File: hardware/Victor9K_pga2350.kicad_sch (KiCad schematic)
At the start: 28 parts, among them IC1 74LVC1G14GW,125, J1 PICO DEBUG, J2 Micro_SD_Card, J4 DX07S016JA1R1500, J5 UART, SW1 BOOTSEL, U1 ESP32-S3-DevKitC

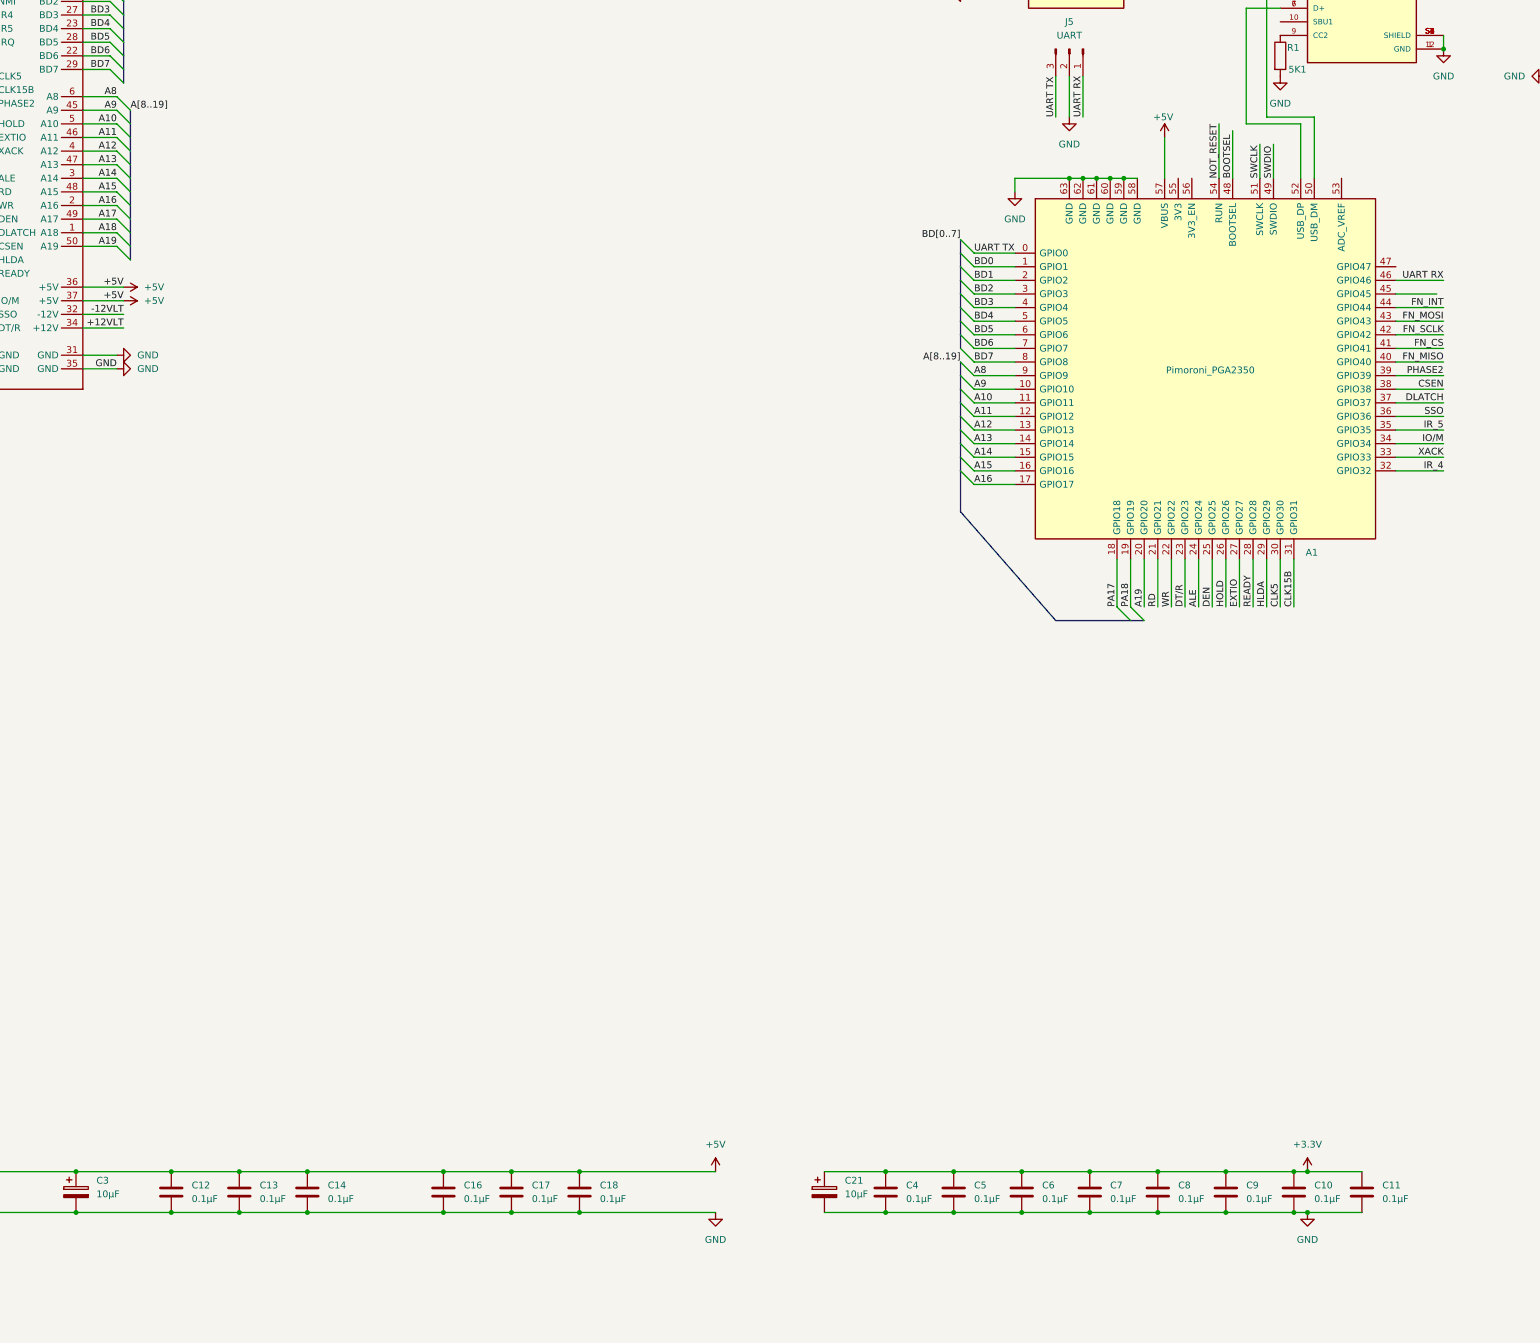
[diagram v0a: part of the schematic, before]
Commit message: initial version of re-worked hardware removing the 74LVC245's
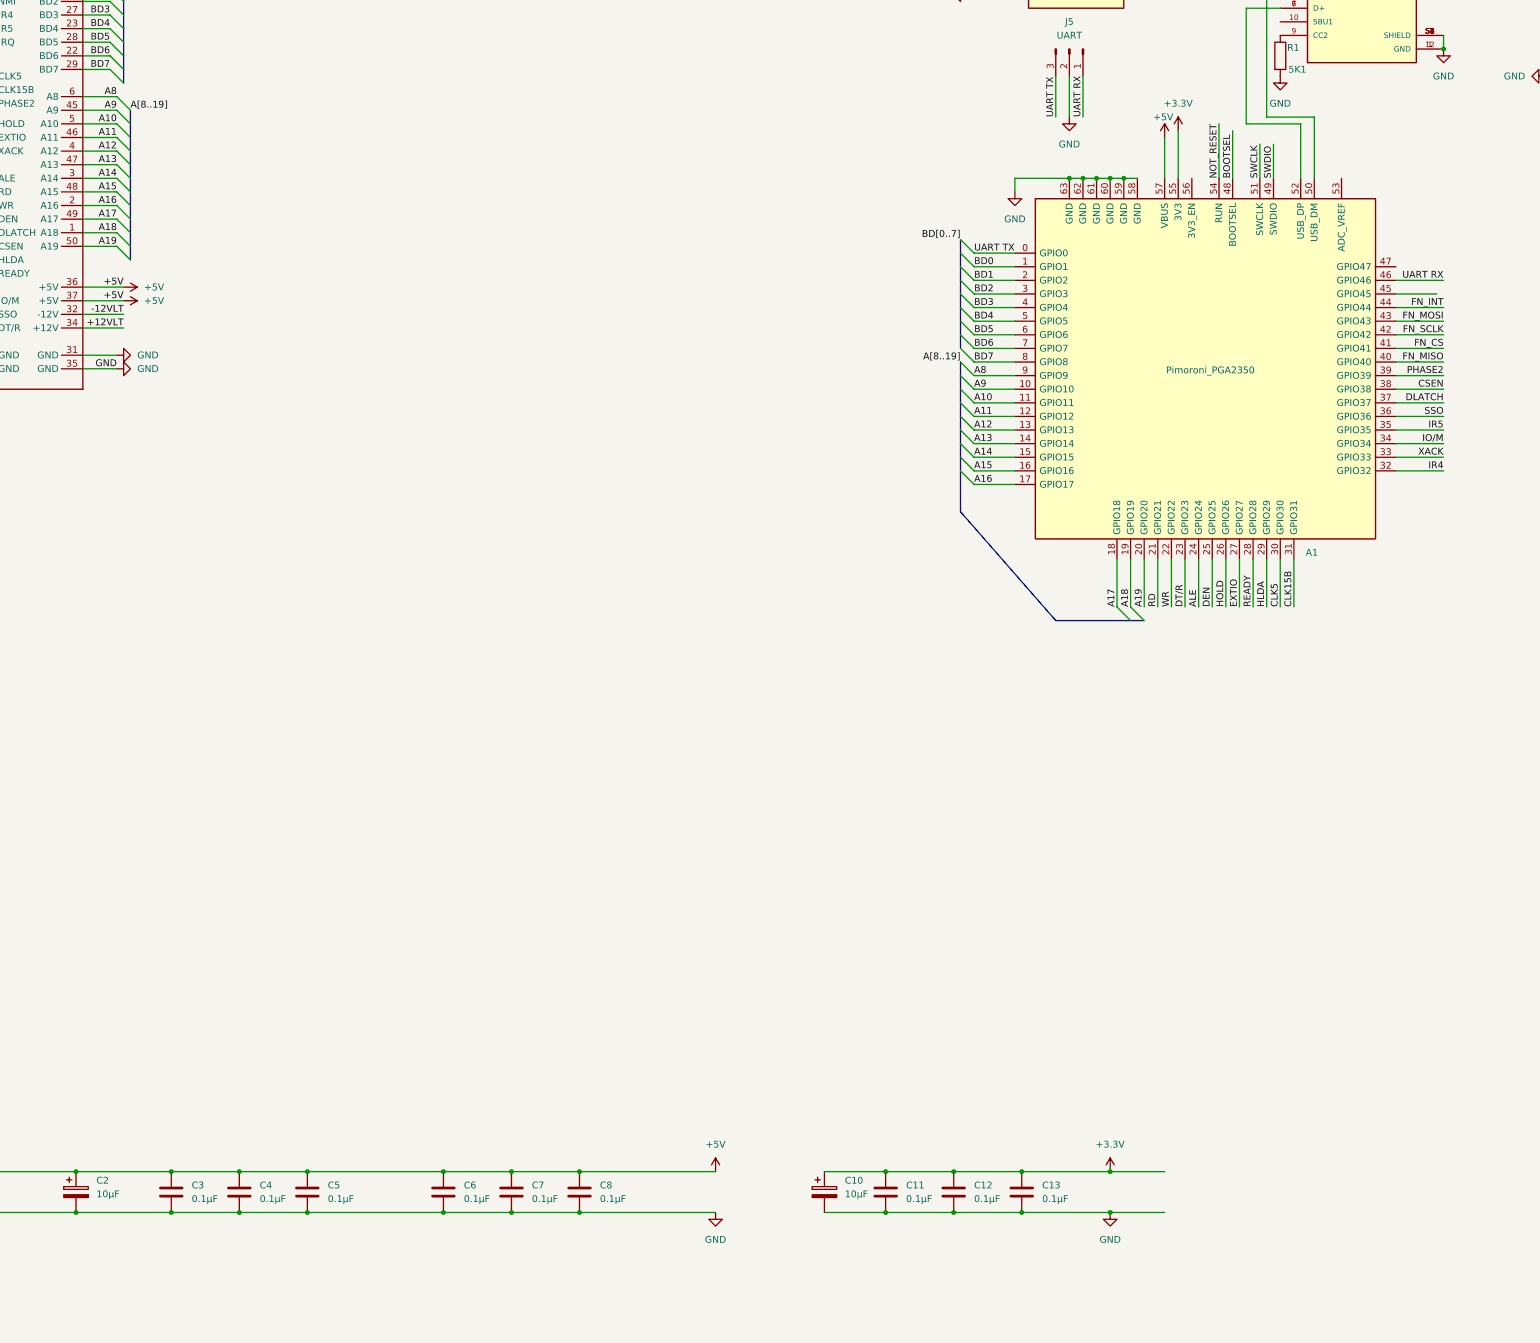
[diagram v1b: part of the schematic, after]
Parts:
- removed C10, C11, C7, C8, C9: 0.1µF, Capacitor_THT:C_Disc_D5.0mm_W2.5mm_P5.00mm, symbol Device:C
- C10: renamed from C21; footprint Capacitor_THT:CP_Axial_L10.0mm_D4.5mm_P15.00mm_Horizontal -> Capacitor_THT:C_Disc_D5.0mm_W2.5mm_P5.00mm
- GF1: footprint Victor9000:Victor Gold Fingers 3 -> Victor9000:Victor_Gold_Fingers_3
- renumbered C4 to C11, C5 to C12, C6 to C13, C3 to C2, C12 to C3, C13 to C4, C14 to C5, C16 to C6, C17 to C7, C18 to C8
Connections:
- net IR_4 is gone; now on net IR4: A1.32 (GPIO32)
- net IR_5 is gone; now on net IR5: A1.35 (GPIO35)
- net PA17 is gone; now on net A17: A1.18 (GPIO18)
- net PA18 is gone; now on net A18: A1.19 (GPIO19)
- net +3.3V: now also A1.55 (3V3)
